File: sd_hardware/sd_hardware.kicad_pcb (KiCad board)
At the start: 2 copper layers, 103 x 70.5 mm, 87 parts, among them IC1 TJA1441AT, IC101 BD9E201FP4-Z, J1 Conn_01x02_Socket, J10 RJ45, J11 XT60PW-M_1x02_Horizontal, J12 Conn_01x02_Socket, J2 Conn_01x02_Socket, J3 Conn_01x02_Socket, J301 STLink-v3mini, J4 Conn_01x02_Socket, J5 Conn_01x02_Socket, J6 Conn_01x02_Socket, J7 Conn_01x02_Socket, J8 Conn_01x02_Socket, J9 RJ45, Q1 RD3L08BGNTL, Q2 RD3L08BGNTL, Q3 RD3L08BGNTL, Q4 RD3L08BGNTL, Q5 RD3L08BGNTL, Q6 RD3L08BGNTL, Q7 RD3L08BGNTL, Q8 RD3L08BGNTL, SW1 SW_DIP_x03, SW301 SW_Push, U1 TLP291, U2 TLP291, U3 TLP291, U301 STM32G431K8Tx, U4 TLP291, U5 TLP291, U6 TLP291, U7 TLP291, U8 TLP291

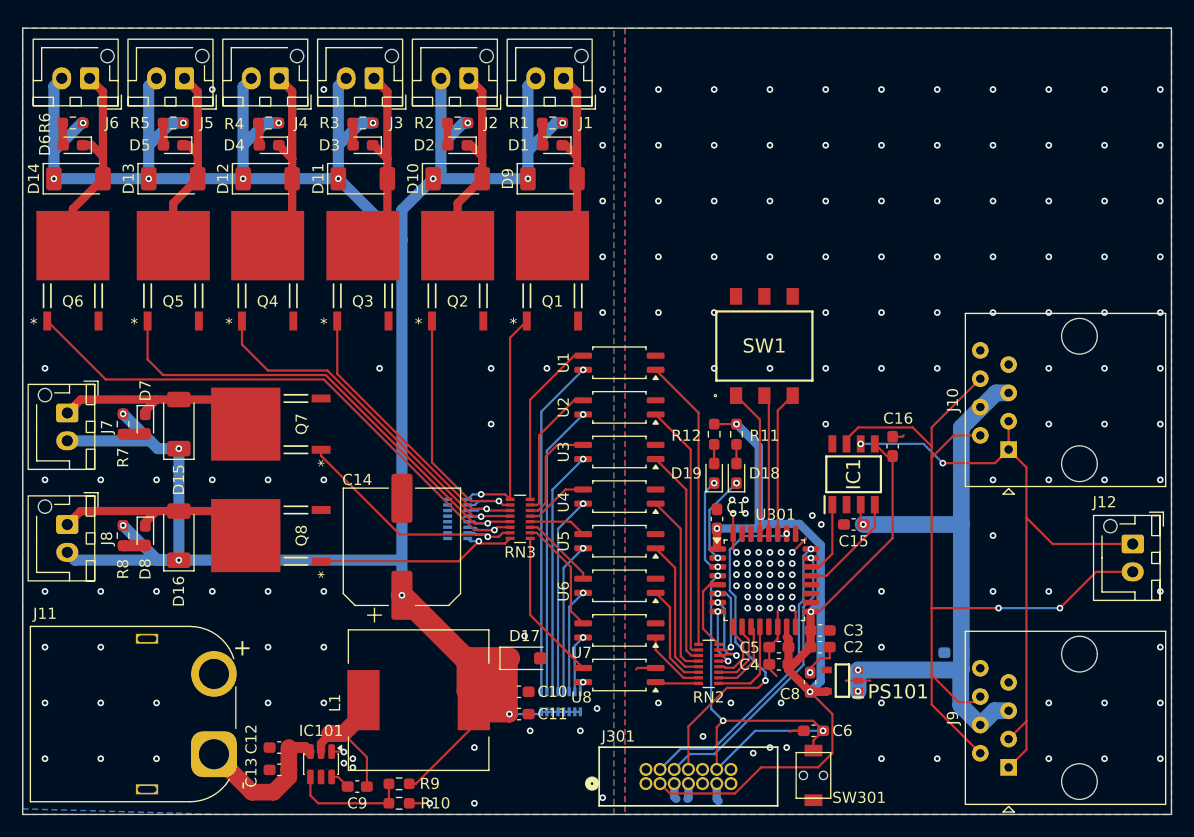
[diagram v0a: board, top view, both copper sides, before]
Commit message: fix var3.0 sd_hardware
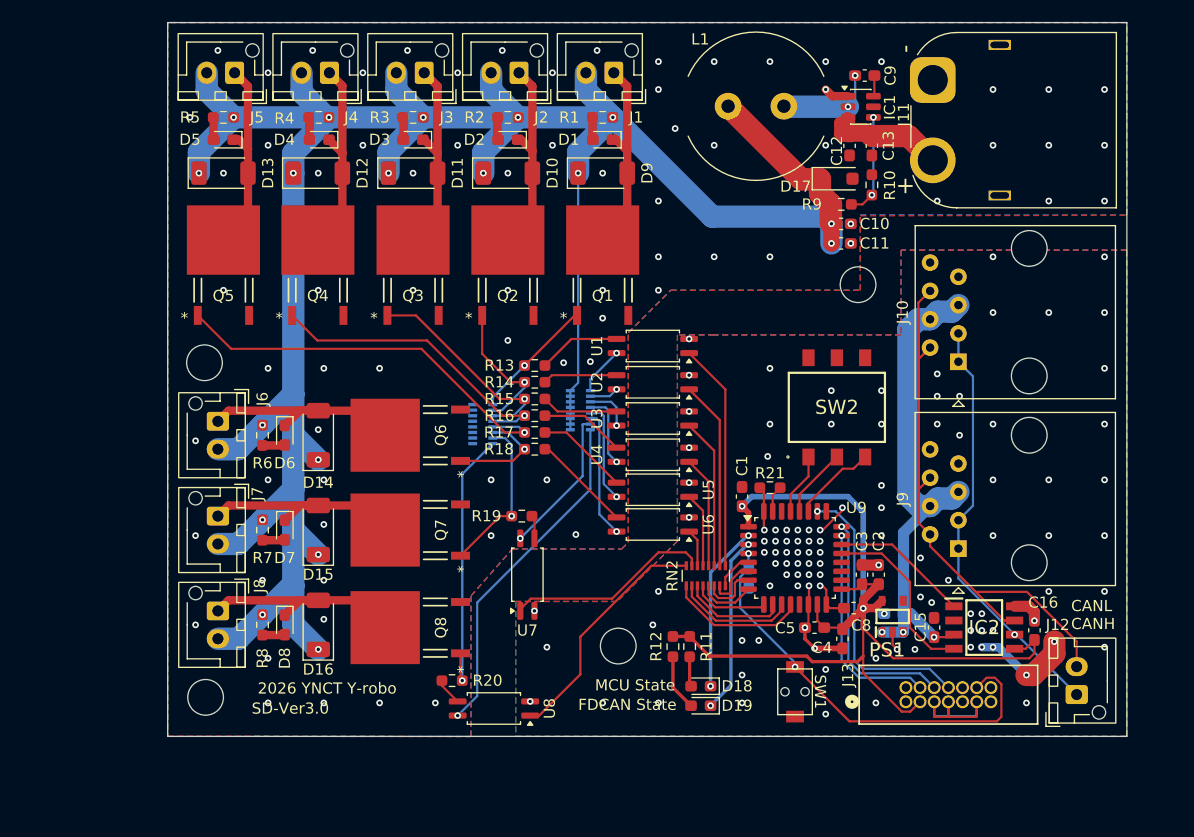
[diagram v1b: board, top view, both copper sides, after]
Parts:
- removed C14: 680μ, Capacitor_SMD:CP_Elec_10x12.6
- removed the RN3 at (127.6, 103.5)
- added R13: 120, Resistor_SMD:R_0603_1608Metric_Pad0.98x0.95mm_HandSolder, F.Cu at (128.9, 89.8)
- added R14: 120, Resistor_SMD:R_0603_1608Metric_Pad0.98x0.95mm_HandSolder, F.Cu at (128.9, 91.2)
- added R15: 120, Resistor_SMD:R_0603_1608Metric_Pad0.98x0.95mm_HandSolder, F.Cu at (128.9, 92.7)
- added R16: 120, Resistor_SMD:R_0603_1608Metric_Pad0.98x0.95mm_HandSolder, F.Cu at (128.9, 94.2)
- added R17: 120, Resistor_SMD:R_0603_1608Metric_Pad0.98x0.95mm_HandSolder, F.Cu at (128.9, 95.8)
- added R18: 120, Resistor_SMD:R_0603_1608Metric_Pad0.98x0.95mm_HandSolder, F.Cu at (128.9, 97.2)
- added R19: 120, Resistor_SMD:R_0603_1608Metric_Pad0.98x0.95mm_HandSolder, F.Cu at (127.8, 103.2)
- added R20: 120, Resistor_SMD:R_0603_1608Metric_Pad0.98x0.95mm_HandSolder, F.Cu at (121.5, 118.0)
- added R21: 10k, Resistor_SMD:R_0603_1608Metric_Pad0.98x0.95mm_HandSolder, F.Cu at (150.0, 100.7)
- added REF**: Y-robo_logo, y-robo_footprint:Y-robo_logo, B.Cu at (107.1, 69.7)
- C6: moved to B.Cu
- D17: value SMF24VTF -> SMF15VTF
- L1: footprint Inductor_SMD:L_12x12mm_H4.5mm -> y-robo_footprint:RP1315BNP-220M
- R1, R2, R3, R4, R5, R6, R7, R8: value 1k -> 1.5k
- moved J11 88.4 mm to (164.6, 64.2), turned to -90 degrees
- moved C9 78.3 mm to (158.5, 63.8), turned to 0 degrees
- moved C13 77.2 mm to (159.1, 70.0), turned to -90 degrees
- moved IC1 76.3 mm to (158.1, 66.5), turned to 0 degrees
- moved C12 74.3 mm to (157.1, 70.0), turned to -90 degrees
- moved R10 69.8 mm to (159.1, 73.5), turned to 90 degrees
- moved R9 65.3 mm to (156.4, 75.3), turned to 0 degrees
- moved L1 61.2 mm to (148.8, 66.5), turned to 0 degrees
- moved D17 51.3 mm to (156.0, 73.0)
- moved C11 51.1 mm to (156.4, 78.8)
- moved C10 50.9 mm to (156.4, 77.0)
- moved J6 32.8 mm to (100.5, 94.8), turned to -90 degrees
- moved Q6 32.8 mm to (115.5, 96.0), turned to 90 degrees
- moved R6 32.8 mm to (104.5, 96.0), turned to 90 degrees
- moved D6 32.2 mm to (106.5, 96.0), turned to -90 degrees
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- renumbered IC101 to IC1, IC1 to IC2, J301 to J13, PS101 to PS1, RN4 to RN3, SW301 to SW1, SW1 to SW2, U301 to U9
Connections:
- J11 pad 1: +24V -> GNDPWR
- J11 pad 2: GNDPWR -> +24V
- U9 pad 23: /MCU_stm32_g431k8t6/JTCK_SWCLK -> /MCU_stm32_g431k8t6/JTMS_SWDIO
- U9 pad 24: /MCU_stm32_g431k8t6/JTMS_SWDIO -> /MCU_stm32_g431k8t6/JTCK_SWCLK
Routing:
- net +12V: track 284.8 -> 233.0 mm
- net /Solenoid_Isolation/FET6_Gate: track 51.9 -> 9.65 mm
- net Net-(RN1-R1.2): track 0.97 -> 30.6 mm
- net /CANH: track 76.3 -> 50.2 mm, vias 2 -> 0
- net Net-(RN1-R8.2): track 30.4 -> 4.34 mm
- net Net-(RN1-R7.2): track 26.2 -> 2.60 mm
- net /CANL: track 59.6 -> 38.0 mm, vias 2 -> 1
- net GND: track 28.6 -> 50.2 mm, vias 129 -> 107
- net Net-(RN1-R6.2): track 22.0 -> 4.19 mm
- net Net-(RN2-R1.2): track 3.90 -> 21.5 mm
- net Net-(RN2-R2.2): track 6.00 -> 18.5 mm
- net +5V: track 57.4 -> 45.4 mm
- net /Solenoid_Isolation/FET2_Gate: track 24.3 -> 12.5 mm
- net Net-(RN1-R5.2): track 17.8 -> 6.65 mm
- net Net-(R20-Pad2): track 13.6 -> 2.45 mm
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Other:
- board size 103 x 70.5 mm -> 86 x 64 mm
- board text added: "2026 YNCT Y-robo"
- board text added: "CANL CANH"
- board text added: "FDCAN State"
- board text added: "MCU State"
- board text added: "SD-Ver3.0"

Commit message: created schematic
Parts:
- removed the C1 at (147.5, 101.5)
- removed the C2 at (159.8, 108.5)
- removed the C3 at (158.2, 108.5)
- removed the C4 at (156.5, 114.2)
- removed the C5 at (154.0, 113.2)
- removed the D3 at (118.0, 69.5)
- removed the IC1 at (158.1, 66.5)
- removed the L1 at (148.8, 66.5)
- removed Q1, Q2, Q3, Q4, Q5, Q6, Q7, Q8: RD3L08BGNTL, y-robo_footprint:TO252-3_ROM
- removed the R3 at (118.0, 67.5)
- removed the R4 at (109.5, 67.5)
- removed REF**: Y-robo_logo, y-robo_footprint:Y-robo_logo
- removed RN1: 1k_x8, Resistor_SMD:R_Array_Convex_8x0602
- removed RN2: 330_x8, Resistor_SMD:R_Array_Convex_8x0602
- removed RN3: 10k_x08, Resistor_SMD:R_Array_Convex_8x0602
- removed U7, U8: TLP291, Package_SO:SOIC-4_4.55x2.6mm_P1.27mm
- removed U9: STM32G431K8Tx, Package_QFP:LQFP-32_7x7mm_P0.8mm
- added C1: 0.1μ, Capacitor_SMD:C_0603_1608Metric_Pad1.08x0.95mm_HandSolder, F.Cu at (20.2, 123.0)
- added C1: 0.1μ, Capacitor_SMD:C_0603_1608Metric_Pad1.08x0.95mm_HandSolder, F.Cu at (94.8, 2.75)
- added C14: 0.1μ, Capacitor_SMD:C_0603_1608Metric_Pad1.08x0.95mm_HandSolder, F.Cu at (76.6, 66.9)
- added C17: 1μ, Capacitor_SMD:C_0603_1608Metric_Pad1.08x0.95mm_HandSolder, F.Cu at (72.5, 122.3)
- added C18: 220nF, Capacitor_SMD:C_0603_1608Metric_Pad1.08x0.95mm_HandSolder, F.Cu at (72.5, 124.8)
- added C19: 0.1μ, Capacitor_SMD:C_0603_1608Metric_Pad1.08x0.95mm_HandSolder, F.Cu at (72.5, 100.2)
- added C2: 22μ, Capacitor_SMD:C_0603_1608Metric_Pad1.08x0.95mm_HandSolder, F.Cu at (20.2, 125.5)
- added C2: 22μ, Capacitor_SMD:C_0603_1608Metric_Pad1.08x0.95mm_HandSolder, F.Cu at (92.6, 16.1)
- added C20: 0.1μ, Capacitor_SMD:C_0603_1608Metric_Pad1.08x0.95mm_HandSolder, F.Cu at (72.5, 102.7)
- added C21: 0.1μ, Capacitor_SMD:C_0603_1608Metric_Pad1.08x0.95mm_HandSolder, F.Cu at (76.6, 43.3)
- added C22: 0.1μ, Capacitor_SMD:C_0603_1608Metric_Pad1.08x0.95mm_HandSolder, F.Cu at (76.6, 45.8)
- added C23: 10nF, Capacitor_SMD:C_0603_1608Metric_Pad1.08x0.95mm_HandSolder, F.Cu at (76.6, 48.3)
- added C3: 22μ, Capacitor_SMD:C_0603_1608Metric_Pad1.08x0.95mm_HandSolder, F.Cu at (20.2, 128.0)
- added C3: 22μ, Capacitor_SMD:C_0603_1608Metric_Pad1.08x0.95mm_HandSolder, F.Cu at (92.6, 17.8)
- added C4: 0.1μ, Capacitor_SMD:C_0603_1608Metric_Pad1.08x0.95mm_HandSolder, F.Cu at (20.2, 130.5)
- added C4: 0.1μ, Capacitor_SMD:C_0603_1608Metric_Pad1.08x0.95mm_HandSolder, F.Cu at (93.4, 9.05)
- added C5: 10μ, Capacitor_SMD:C_0603_1608Metric_Pad1.08x0.95mm_HandSolder, F.Cu at (95.4, 9.05)
- added C5: 10μ, Capacitor_SMD:C_0603_1608Metric_Pad1.08x0.95mm_HandSolder, F.Cu at (20.2, 133.0)
- added D3: SMF15VTF, Diode_SMD:D_SOD-123F, F.Cu at (92.2, 12.0)
- added D3: SMF15VTF, Diode_SMD:D_SOD-123F, F.Cu at (44.2, 131.2)
- added IC1: BD9E201FP4-Z, Package_TO_SOT_SMD:TSOT-23-6, F.Cu at (94.4, 5.55)
- added IC1: BD9E201FP4-Z, Package_TO_SOT_SMD:TSOT-23-6, F.Cu at (38.9, 131.9)
- added IC10: TJA1441AT, y-robo_footprint:SOIC127P600X175-8N, F.Cu at (78.7, 62.3)
- added IC3: TLP170AM_TPL,E, y-robo_footprint:TLP170AMTPLE, F.Cu at (28.2, 47.3)
- added IC4: TLP170AM_TPL,E, y-robo_footprint:TLP170AMTPLE, F.Cu at (35.0, 47.3)
- added IC5: TLP170AM_TPL,E, y-robo_footprint:TLP170AMTPLE, F.Cu at (41.8, 47.3)
- added IC6: TLP170AM_TPL,E, y-robo_footprint:TLP170AMTPLE, F.Cu at (48.6, 47.3)
- added IC7: TLP170AM_TPL,E, y-robo_footprint:TLP170AMTPLE, F.Cu at (55.4, 47.3)
- added IC8: TLP170AM_TPL,E, y-robo_footprint:TLP170AMTPLE, F.Cu at (62.2, 47.3)
- added IC9: TLP170AM_TPL,E, y-robo_footprint:TLP170AMTPLE, F.Cu at (69.0, 47.3)
- added J14: STLink-v3mini, y-robo_footprint:CONN14_3220-14_CNC, F.Cu at (84.4, 93.3)
- added L1: 22μ, y-robo_footprint:RP1315BNP-220M, F.Cu at (85.0, 5.50)
- added L1: 22μ, y-robo_footprint:RP1315BNP-220M, F.Cu at (60.7, 109.3)
- added R22: 1.5k, Resistor_SMD:R_0603_1608Metric_Pad0.98x0.95mm_HandSolder, F.Cu at (38.4, 61.7)
- added R23: 10k, Resistor_SMD:R_0603_1608Metric_Pad0.98x0.95mm_HandSolder, F.Cu at (38.4, 64.2)
- added R24: 10k, Resistor_SMD:R_0603_1608Metric_Pad0.98x0.95mm_HandSolder, F.Cu at (38.4, 66.8)
- added R25: 10k, Resistor_SMD:R_0603_1608Metric_Pad0.98x0.95mm_HandSolder, F.Cu at (42.7, 54.2)
- added R26: 10k, Resistor_SMD:R_0603_1608Metric_Pad0.98x0.95mm_HandSolder, F.Cu at (42.7, 56.7)
- added R27: 10k, Resistor_SMD:R_0603_1608Metric_Pad0.98x0.95mm_HandSolder, F.Cu at (42.7, 59.2)
- added R28: 10k, Resistor_SMD:R_0603_1608Metric_Pad0.98x0.95mm_HandSolder, F.Cu at (42.7, 61.7)
- added R29: 10k, Resistor_SMD:R_0603_1608Metric_Pad0.98x0.95mm_HandSolder, F.Cu at (42.7, 64.2)
- added R3: 100k, Resistor_SMD:R_0603_1608Metric_Pad0.98x0.95mm_HandSolder, F.Cu at (24.5, 133.0)
- added R3: 100k, Resistor_SMD:R_0603_1608Metric_Pad0.98x0.95mm_HandSolder, F.Cu at (92.6, 14.3)
- added R30: 10k, Resistor_SMD:R_0603_1608Metric_Pad0.98x0.95mm_HandSolder, F.Cu at (42.7, 66.8)
- added R31: 10k, Resistor_SMD:R_0603_1608Metric_Pad0.98x0.95mm_HandSolder, F.Cu at (72.5, 94.9)
- added R32: 0, Resistor_SMD:R_0603_1608Metric_Pad0.98x0.95mm_HandSolder, F.Cu at (72.5, 127.3)
- added R33: 0, Resistor_SMD:R_0603_1608Metric_Pad0.98x0.95mm_HandSolder, F.Cu at (72.5, 129.8)
- added R34: 40k, Resistor_SMD:R_0603_1608Metric_Pad0.98x0.95mm_HandSolder, F.Cu at (72.5, 132.3)
- added R35: 40k, Resistor_SMD:R_0603_1608Metric_Pad0.98x0.95mm_HandSolder, F.Cu at (76.8, 119.8)
- added R36: 0, Resistor_SMD:R_0603_1608Metric_Pad0.98x0.95mm_HandSolder, F.Cu at (76.8, 122.3)
- added R37: 10k, Resistor_SMD:R_0603_1608Metric_Pad0.98x0.95mm_HandSolder, F.Cu at (76.8, 124.8)
- added R38: 0, Resistor_SMD:R_0603_1608Metric_Pad0.98x0.95mm_HandSolder, F.Cu at (76.8, 127.3)
- added R39: 10k, Resistor_SMD:R_0603_1608Metric_Pad0.98x0.95mm_HandSolder, F.Cu at (76.8, 129.8)
- added R4: 5.23k, Resistor_SMD:R_0603_1608Metric_Pad0.98x0.95mm_HandSolder, F.Cu at (28.9, 123.0)
- added R4: 5.23k, Resistor_SMD:R_0603_1608Metric_Pad0.98x0.95mm_HandSolder, F.Cu at (95.4, 12.6)
- added R40: 10k, Resistor_SMD:R_0603_1608Metric_Pad0.98x0.95mm_HandSolder, F.Cu at (72.5, 105.2)
- added R41: 10k, Resistor_SMD:R_0603_1608Metric_Pad0.98x0.95mm_HandSolder, F.Cu at (72.5, 107.7)
- added R42: 0, Resistor_SMD:R_0603_1608Metric_Pad0.98x0.95mm_HandSolder, F.Cu at (72.5, 110.3)
- added R43: 0, Resistor_SMD:R_0603_1608Metric_Pad0.98x0.95mm_HandSolder, F.Cu at (72.5, 112.8)
- added R44: 0, Resistor_SMD:R_0603_1608Metric_Pad0.98x0.95mm_HandSolder, F.Cu at (72.5, 115.3)
- added R45: 100k, Resistor_SMD:R_0603_1608Metric_Pad0.98x0.95mm_HandSolder, F.Cu at (76.6, 50.8)
- added R46: 100, Resistor_SMD:R_0603_1608Metric_Pad0.98x0.95mm_HandSolder, F.Cu at (76.6, 53.3)
- added R47: 100k, Resistor_SMD:R_0603_1608Metric_Pad0.98x0.95mm_HandSolder, F.Cu at (76.6, 55.8)
- C10: value 22μ -> 100n
- C11: value 22μ -> 1μ
- C12: value 0.1μ -> 10n
- C13: value 10μ -> 0.1μ
- C15: value 0.1μ -> 0.1u
- C16: value 0.1u -> 0.1μ
- C6: value 0.1μ -> 1μ; moved to F.Cu
- C7: moved to F.Cu
- C8: value 1μ -> 100n
- C9: value 0.1μ -> 4.7μ
- D10, D12, D14, D16: value RB055LAM-40TR -> LED; footprint Diode_SMD:D_SOD-128 -> LED_SMD:LED_0603_1608Metric_Pad1.05x0.95mm_HandSolder
- D11, D13, D15, D9: value RB055LAM-40TR -> RB520VM-40; footprint Diode_SMD:D_SOD-128 -> Diode_SMD:D_SOD-323_HandSoldering
- D17: value SMF15VTF -> RB520VM-40; footprint Diode_SMD:D_SOD-123F -> Diode_SMD:D_SOD-323_HandSoldering
- D19, D5, D7: value LED -> RB520VM-40; footprint LED_SMD:LED_0603_1608Metric_Pad1.05x0.95mm_HandSolder -> Diode_SMD:D_SOD-323_HandSoldering
- IC2: value TJA1441AT -> TLP170AM_TPL,E; footprint y-robo_footprint:SOIC127P600X175-8N -> y-robo_footprint:TLP170AMTPLE
- J1: footprint Connector_JST:JST_XH_B2B-XH-AM_1x02_P2.50mm_Vertical -> Connector_JST:JST_XH_B2B-XH-A_1x02_P2.50mm_Vertical
- J10: value RJ45 -> Conn_01x06_Socket; footprint Connector_RJ:RJ45_Amphenol_54602-x08_Horizontal -> Connector_JST:JST_XH_B6B-XH-A_1x06_P2.50mm_Vertical
- J11: value XT60PW-M_1x02_Horizontal -> Conn_01x02_Socket; footprint Connector_AMASS:AMASS_XT60PW-M_1x02_P7.20mm_Horizontal -> Connector_JST:JST_XH_B2B-XH-AM_1x02_P2.50mm_Vertical
- J12: value Conn_01x02_Socket -> RJ45; footprint Connector_JST:JST_XH_B2B-XH-AM_1x02_P2.50mm_Vertical -> Connector_RJ:RJ45_Amphenol_54602-x08_Horizontal
- J13: value STLink-v3mini -> RJ45; footprint y-robo_footprint:CONN14_3220-14_CNC -> Connector_RJ:RJ45_Amphenol_54602-x08_Horizontal
- J8: value Conn_01x02_Socket -> XT60PW-M_1x02_Horizontal; footprint Connector_JST:JST_XH_B2B-XH-AM_1x02_P2.50mm_Vertical -> Connector_AMASS:AMASS_XT60PW-M_1x02_P7.20mm_Horizontal
- J9: value RJ45 -> Conn_01x02_Socket; footprint Connector_RJ:RJ45_Amphenol_54602-x08_Horizontal -> Connector_JST:JST_XH_B2B-XH-AM_1x02_P2.50mm_Vertical
- R1, R2: value 1.5k -> 1k
- R10: value 5.23k -> 680
- R11, R12: value 1k -> 680
- R13, R14, R15, R16: value 120 -> 680
- R17, R18, R19, R20: value 120 -> 1.5k
- R21: value 10k -> 1.5k
- R5, R6: value 1.5k -> 0
- R9: value 100k -> 680
- SW1: value SW_Push -> SW_DIP_x03; footprint y-robo_footprint:TVAF06-A020B-R -> y-robo_footprint:DS04-254-2-03BK-SMT
- SW2: value SW_DIP_x03 -> SW_Push; footprint y-robo_footprint:DS04-254-2-03BK-SMT -> y-robo_footprint:TVAF06-A020B-R
- U1: value TLP291 -> STM32G431K8Tx; footprint Package_SO:SOIC-4_4.55x2.6mm_P1.27mm -> Package_QFP:LQFP-32_7x7mm_P0.8mm
- U2: value TLP291 -> DAC60501ZDGSR; footprint Package_SO:SOIC-4_4.55x2.6mm_P1.27mm -> y-robo_footprint:DGS10_TEX
- U3: value TLP291 -> BD87521G-LB; footprint Package_SO:SOIC-4_4.55x2.6mm_P1.27mm -> y-robo_footprint:SOT95P280X125-5N
- U4: value TLP291 -> ADUM251N1BRIZ; footprint Package_SO:SOIC-4_4.55x2.6mm_P1.27mm -> y-robo_footprint:ADUM251N1BRIZ_ADI
- U5: value TLP291 -> BD87581YG-C; footprint Package_SO:SOIC-4_4.55x2.6mm_P1.27mm -> y-robo_footprint:SOT95P280X125-5N
- U6: value TLP291 -> ADS1018IDGSR; footprint Package_SO:SOIC-4_4.55x2.6mm_P1.27mm -> y-robo_footprint:DGS10_TEX
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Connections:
- C10 pad 1: +12V -> +3.3V
- C10 pad 2: GNDPWR -> GND
- C11 pad 1: +12V -> +3.3V
- C11 pad 2: GNDPWR -> GND
- C12 pad 1: +24V -> +3.3V
- C12 pad 2: GNDPWR -> GND
- C13 pad 1: +24V -> /MCU_stm32_g431k8t6/NRST
- C13 pad 2: GNDPWR -> GND
- C15 pad 1: +5V -> +3.3V
- C16 pad 1: +3.3V -> +12V
- C16 pad 2: GND -> GNDPWR
- C6 pad 1: /MCU_stm32_g431k8t6/NRST -> +5V
- C7 pad 1: +5V -> +3.3V
- C9 pad 1: Net-(IC1-SW) -> +3.3V
- C9 pad 2: Net-(IC1-BOOT) -> GND
- D1 pad 1: /Solenoid_Isolation/Solenoid1_- -> /MCU_stm32_g431k8t6/MCU_State_LED
- D10 pad 1: +12V -> /Solenoid_Iso/PhotoRelay6_Drain
- D10 pad 2: /Solenoid_Isolation/Solenoid2_- -> Net-(D10-A)
- D11 pad 2: /Solenoid_Isolation/Solenoid3_- -> /Solenoid_Iso/PhotoRelay6_Drain
- D12 pad 1: +12V -> /Solenoid_Iso/PhotoRelay3_Drain
- D12 pad 2: /Solenoid_Isolation/Solenoid4_- -> Net-(D12-A)
- D13 pad 2: /Solenoid_Isolation/Solenoid5_- -> /Solenoid_Iso/PhotoRelay3_Drain
- D14 pad 1: +12V -> /Solenoid_Iso/PhotoRelay7_Drain
- D14 pad 2: /Solenoid_Isolation/Solenoid6_- -> Net-(D14-A)
- D15 pad 2: /Solenoid_Isolation/Solenoid7_- -> /Solenoid_Iso/PhotoRelay7_Drain
- D16 pad 1: +12V -> /Solenoid_Iso/PhotoRelay4_Drain
- D16 pad 2: /Solenoid_Isolation/Solenoid8_- -> Net-(D16-A)
- D17 pad 2: GNDPWR -> /Solenoid_Iso/PhotoRelay4_Drain
- D18 pad 1: /MCU_stm32_g431k8t6/MCU_State_LED -> /Solenoid_Iso/PhotoRelay8_Drain
- D19 pad 1: /MCU_stm32_g431k8t6/FDCAN1_LED -> +12V
- D19 pad 2: Net-(D19-A) -> /Solenoid_Iso/PhotoRelay8_Drain
- D2 pad 1: /Solenoid_Isolation/Solenoid2_- -> /MCU_stm32_g431k8t6/FDCAN1_LED
- D4 pad 1: /Solenoid_Isolation/Solenoid4_- -> /Solenoid_Iso/PhotoRelay1_Drain
- D5 pad 1: /Solenoid_Isolation/Solenoid5_- -> +12V
- D5 pad 2: Net-(D5-A) -> /Solenoid_Iso/PhotoRelay1_Drain
- D6 pad 1: /Solenoid_Isolation/Solenoid6_- -> /Solenoid_Iso/PhotoRelay5_Drain
- D7 pad 1: /Solenoid_Isolation/Solenoid7_- -> +12V
- D7 pad 2: Net-(D7-A) -> /Solenoid_Iso/PhotoRelay5_Drain
- D8 pad 1: /Solenoid_Isolation/Solenoid8_- -> /Solenoid_Iso/PhotoRelay2_Drain
- D9 pad 2: /Solenoid_Isolation/Solenoid1_- -> /Solenoid_Iso/PhotoRelay2_Drain
- IC2 pad 1: /FDCAN_Transceiver/CAN_TX -> Net-(IC2-A)
- IC2 pad 3: +5V -> GND
- IC2 pad 4: /FDCAN_Transceiver/CAN_RX -> GNDPWR
- IC2 pad 6: /CANL -> /Solenoid_Iso/PhotoRelay1_Drain
- J1 pad 1: /Solenoid_Isolation/Solenoid1_- -> /Solenoid_Iso/PhotoRelay1_Drain
- J10 pad 1: /CANL -> +12V
- J10 pad 2: /CANH -> GNDPWR
- J10 pad 3: /CANL -> /SPI_DAC/-VSENSE
- J10 pad 4: +5V -> /SPI_DAC/VOUT
- J10 pad 5: +5V -> /SPI_DAC/+VSENSE
- J10 pad 6: /CANH -> /SPI_ADC/VIN
- J11 pad 1: GNDPWR -> /CANL
- J11 pad 2: +24V -> /CANH
- J13 pad 1: unconnected-(J13-Pin_1-Pad1) -> /CANL
- J13 pad 2: unconnected-(J13-Pin_2-Pad2) -> /CANH
- J13 pad 3: +3.3V -> /CANL
- J13 pad 4: /MCU_stm32_g431k8t6/JTMS_SWDIO -> +5V
- J13 pad 5: GND -> +5V
- J13 pad 6: /MCU_stm32_g431k8t6/JTCK_SWCLK -> /CANH
- J13 pad 8: /MCU_stm32_g431k8t6/JTDO_SWO -> GND
- J2 pad 1: /Solenoid_Isolation/Solenoid2_- -> /Solenoid_Iso/PhotoRelay5_Drain
- J3 pad 1: /Solenoid_Isolation/Solenoid3_- -> /Solenoid_Iso/PhotoRelay2_Drain
- J4 pad 1: /Solenoid_Isolation/Solenoid4_- -> /Solenoid_Iso/PhotoRelay6_Drain
- J5 pad 1: /Solenoid_Isolation/Solenoid5_- -> /Solenoid_Iso/PhotoRelay3_Drain
- J6 pad 1: /Solenoid_Isolation/Solenoid6_- -> /Solenoid_Iso/PhotoRelay7_Drain
- J7 pad 1: /Solenoid_Isolation/Solenoid7_- -> /Solenoid_Iso/PhotoRelay4_Drain
- J8 pad 1: /Solenoid_Isolation/Solenoid8_- -> GNDPWR
- J8 pad 2: +12V -> +24V
- J9 pad 1: /CANL -> /Solenoid_Iso/PhotoRelay8_Drain
- J9 pad 2: /CANH -> +12V
- R1 pad 1: Net-(D1-A) -> +3.3V
- R1 pad 2: +12V -> Net-(D1-A)
- R10 pad 1: /FB -> /MCU_stm32_g431k8t6/Solenoid2_GPIO
- R10 pad 2: GNDPWR -> Net-(IC3-A)
- R11 pad 1: +3.3V -> /MCU_stm32_g431k8t6/Solenoid3_GPIO
- R11 pad 2: Net-(D18-A) -> Net-(IC4-A)
- R12 pad 1: +3.3V -> /MCU_stm32_g431k8t6/Solenoid4_GPIO
- R12 pad 2: Net-(D19-A) -> Net-(IC5-A)
- R13 pad 1: /Solenoid_Isolation/FET1_Gate -> /MCU_stm32_g431k8t6/Solenoid5_GPIO
- R13 pad 2: Net-(R13-Pad2) -> Net-(IC6-A)
- R14 pad 1: /Solenoid_Isolation/FET2_Gate -> /MCU_stm32_g431k8t6/Solenoid6_GPIO
- R14 pad 2: Net-(R14-Pad2) -> Net-(IC7-A)
- R15 pad 1: /Solenoid_Isolation/FET3_Gate -> /MCU_stm32_g431k8t6/Solenoid7_GPIO
- R15 pad 2: Net-(R15-Pad2) -> Net-(IC8-A)
- R16 pad 1: /Solenoid_Isolation/FET4_Gate -> /MCU_stm32_g431k8t6/Solenoid8_GPIO
- R16 pad 2: Net-(R16-Pad2) -> Net-(IC9-A)
- R17 pad 1: /Solenoid_Isolation/FET5_Gate -> Net-(D8-A)
- R17 pad 2: Net-(R17-Pad2) -> +12V
- R18 pad 1: /Solenoid_Isolation/FET6_Gate -> Net-(D10-A)
- R18 pad 2: Net-(R18-Pad2) -> +12V
- R19 pad 1: /Solenoid_Isolation/FET7_Gate -> Net-(D12-A)
- R19 pad 2: Net-(R19-Pad2) -> +12V
- R2 pad 1: Net-(D2-A) -> +3.3V
- R2 pad 2: +12V -> Net-(D2-A)
- R20 pad 1: /Solenoid_Isolation/FET8_Gate -> Net-(D14-A)
- R20 pad 2: Net-(R20-Pad2) -> +12V
- R21 pad 1: /MCU_stm32_g431k8t6/BOOT0 -> Net-(D16-A)
- R21 pad 2: GND -> +12V
- R5 pad 1: Net-(D5-A) -> /MCU_stm32_g431k8t6/SPI1_SCK
- R5 pad 2: +12V -> /SPI_Iso/CLK_IN
- R6 pad 1: Net-(D6-A) -> /MCU_stm32_g431k8t6/SPI1_MOSI
- R6 pad 2: +12V -> /SPI_Iso/MOSI_IN
- R7 pad 1: Net-(D7-A) -> Net-(D4-A)
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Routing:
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- removed copper zone on B.Cu, net GND
- removed copper zone on F.Cu, net GND
- removed copper zone on B.Cu, net GNDPWR
- removed copper zone on F.Cu, net GNDPWR
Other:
- board outline removed
- board text removed: "2026 YNCT Y-robo"
- board text removed: "CANL CANH"
- board text removed: "FDCAN State"
- board text removed: "MCU State"
- board text removed: "SD-Ver3.0"

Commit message: working
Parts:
- removed the C1 at (20.2, 123.0)
- removed the C1 at (94.8, 2.75)
- removed the C2 at (20.2, 125.5)
- removed the C2 at (92.6, 16.1)
- removed the C3 at (20.2, 128.0)
- removed the C3 at (92.6, 17.8)
- removed the C4 at (20.2, 130.5)
- removed the C4 at (93.4, 9.05)
- removed the C5 at (95.4, 9.05)
- removed the C5 at (20.2, 133.0)
- removed the D3 at (92.2, 12.0)
- removed the D3 at (44.2, 131.2)
- removed the IC1 at (94.4, 5.55)
- removed the IC1 at (38.9, 131.9)
- removed the L1 at (85.0, 5.50)
- removed the L1 at (60.7, 109.3)
- removed the R3 at (24.5, 133.0)
- removed the R3 at (92.6, 14.3)
- removed the R4 at (28.9, 123.0)
- removed the R4 at (95.4, 12.6)
- added C1: 0.1μ, Capacitor_SMD:C_0603_1608Metric_Pad1.08x0.95mm_HandSolder, F.Cu at (130.9, 50.0)
- added C2: 0.1μ, Capacitor_SMD:C_0603_1608Metric_Pad1.08x0.95mm_HandSolder, F.Cu at (141.8, 59.0)
- added C24: 0.1μ, Capacitor_SMD:C_0603_1608Metric_Pad1.08x0.95mm_HandSolder, B.Cu at (99.9, 60.8)
- added C25: 10nF, Capacitor_SMD:C_0603_1608Metric_Pad1.08x0.95mm_HandSolder, B.Cu at (96.4, 65.3)
- added C3: 0.1μ, Capacitor_SMD:C_0603_1608Metric_Pad1.08x0.95mm_HandSolder, B.Cu at (123.2, 55.8)
- added C4: 4.7μ, Capacitor_SMD:C_0603_1608Metric_Pad1.08x0.95mm_HandSolder, F.Cu at (141.8, 60.5)
- added C5: 1μ, Capacitor_SMD:C_0603_1608Metric_Pad1.08x0.95mm_HandSolder, F.Cu at (138.1, 62.5)
- added D20: LED, LED_SMD:LED_0603_1608Metric_Pad1.05x0.95mm_HandSolder, F.Cu at (129.2, 73.5)
- added D21: LED, LED_SMD:LED_0603_1608Metric_Pad1.05x0.95mm_HandSolder, F.Cu at (114.0, 73.0)
- added D3: RB520VM-40, Diode_SMD:D_SOD-323_HandSoldering, F.Cu at (144.8, 30.2)
- added IC1: TLP170AM_TPL,E, y-robo_footprint:TLP170AMTPLE, F.Cu at (162.8, 37.8)
- added L1: 22μ, y-robo_footprint:RP1315BNP-220M, F.Cu at (90.5, 41.2)
- added R3: 3.3k, Resistor_SMD:R_0603_1608Metric_Pad0.98x0.95mm_HandSolder, F.Cu at (144.8, 26.2)
- added R4: 3.3k, Resistor_SMD:R_0603_1608Metric_Pad0.98x0.95mm_HandSolder, F.Cu at (135.8, 26.2)
- added R48: 100, Resistor_SMD:R_0603_1608Metric_Pad0.98x0.95mm_HandSolder, B.Cu at (96.4, 63.8)
- added R49: 100k, Resistor_SMD:R_0603_1608Metric_Pad0.98x0.95mm_HandSolder, B.Cu at (101.6, 60.8)
- added R50: 1k, Resistor_SMD:R_0603_1608Metric_Pad0.98x0.95mm_HandSolder, F.Cu at (132.7, 73.5)
- added R51: 1k, Resistor_SMD:R_0603_1608Metric_Pad0.98x0.95mm_HandSolder, F.Cu at (114.0, 71.2)
- added R52: 0, Resistor_SMD:R_0603_1608Metric_Pad0.98x0.95mm_HandSolder, B.Cu at (127.5, 60.8)
- added R53: 0, Resistor_SMD:R_0603_1608Metric_Pad0.98x0.95mm_HandSolder, F.Cu at (111.2, 60.5)
- added R54: 0, Resistor_SMD:R_0603_1608Metric_Pad0.98x0.95mm_HandSolder, F.Cu at (111.2, 62.0)
- added U7: BD00FC0WEFJ, Package_SO:HTSOP-8-1EP_3.9x4.9mm_P1.27mm_EP2.4x3.2mm, B.Cu at (90.8, 52.8)
- C10: value 100n -> 10μ
- C11: value 1μ -> 22μ
- C12: value 10n -> 22μ
- C13, C14: value 0.1μ -> 1μ; moved to B.Cu
- C15: value 0.1u -> 0.1μ
- C16, C7, IC10, PS1, R47, R9, U5, U6: moved to B.Cu
- C17: value 1μ -> 0.1u; moved to B.Cu
- C18: value 220nF -> 0.1μ
- C21: value 0.1μ -> 1μ
- C22: value 0.1μ -> 220nF
- C23: value 10nF -> 0.1μ; moved to B.Cu
- C6: value 1μ -> 10n
- C8: value 100n -> 1μ; moved to B.Cu
- C9: value 4.7μ -> 0.1μ
- D1, D2, D4, D6, D8: value LED -> RB520VM-40; footprint LED_SMD:LED_0603_1608Metric_Pad1.05x0.95mm_HandSolder -> Diode_SMD:D_SOD-323_HandSoldering
- D11, D13, D15, D17, D9: value RB520VM-40 -> LED; footprint Diode_SMD:D_SOD-323_HandSoldering -> LED_SMD:LED_0603_1608Metric_Pad1.05x0.95mm_HandSolder
- D19: value RB520VM-40 -> SMF15VTF; footprint Diode_SMD:D_SOD-323_HandSoldering -> Diode_SMD:D_SOD-123F
- IC9: value TLP170AM_TPL,E -> BD9E201FP4-Z; footprint y-robo_footprint:TLP170AMTPLE -> Package_TO_SOT_SMD:TSOT-23-6
- J10: value Conn_01x06_Socket -> RJ45; footprint Connector_JST:JST_XH_B6B-XH-A_1x06_P2.50mm_Vertical -> Connector_RJ:RJ45_Amphenol_54602-x08_Horizontal
- J11: value Conn_01x02_Socket -> RJ45; footprint Connector_JST:JST_XH_B2B-XH-AM_1x02_P2.50mm_Vertical -> Connector_RJ:RJ45_Amphenol_54602-x08_Horizontal
- J12: value RJ45 -> Conn_01x02_Socket; footprint Connector_RJ:RJ45_Amphenol_54602-x08_Horizontal -> Connector_JST:JST_XH_B2B-XH-A_1x02_P2.50mm_Vertical
- J13: value RJ45 -> XT60PW-M_1x02_Horizontal; footprint Connector_RJ:RJ45_Amphenol_54602-x08_Horizontal -> Connector_AMASS:AMASS_XT60PW-M_1x02_P7.20mm_Horizontal
- J14: value STLink-v3mini -> Conn_01x06_Socket; footprint y-robo_footprint:CONN14_3220-14_CNC -> Connector_JST:JST_XH_B6B-XH-A_1x06_P2.50mm_Vertical
- J2, J3, J4, J5, J6, J7: footprint Connector_JST:JST_XH_B2B-XH-AM_1x02_P2.50mm_Vertical -> Connector_JST:JST_XH_B2B-XH-A_1x02_P2.50mm_Vertical
- J8: value XT60PW-M_1x02_Horizontal -> Conn_01x02_Socket; footprint Connector_AMASS:AMASS_XT60PW-M_1x02_P7.20mm_Horizontal -> Connector_JST:JST_XH_B2B-XH-A_1x02_P2.50mm_Vertical
- J9: value Conn_01x02_Socket -> STLink-v3mini; footprint Connector_JST:JST_XH_B2B-XH-AM_1x02_P2.50mm_Vertical -> y-robo_footprint:CONN14_3220-14_CNC
- R1, R2: value 1k -> 3.3k
- R17: value 1.5k -> 10k; moved to B.Cu
- R18, R19, R20, R21, R22: value 1.5k -> 10k
- R26, R27: value 10k -> 1k
- R28, R29, R31: value 10k -> 0; moved to B.Cu
- R30, R39, R40: value 10k -> 0
- R33: value 0 -> 56.7k; moved to B.Cu
- R34: value 40k -> 10k; moved to B.Cu
- R35: value 40k -> 100k
- R36: value 0 -> 5.23k
- R38, R44: value 0 -> 10k
- R41: value 10k -> 40k; moved to B.Cu
- R42: value 0 -> 40k; moved to B.Cu
- R45: value 100k -> 0
- R46: value 100 -> 10k
- R5, R6: value 0 -> 3.3k
- R7, R8: value 1.5k -> 3.3k
- SW1: value SW_DIP_x03 -> SW_Push; footprint y-robo_footprint:DS04-254-2-03BK-SMT -> y-robo_footprint:TVAF06-A020B-R
- SW2: value SW_Push -> SW_DIP_x03; footprint y-robo_footprint:TVAF06-A020B-R -> y-robo_footprint:DS04-254-2-03BK-SMT
- U2: value DAC60501ZDGSR -> ADUM251N1BRIZ; footprint y-robo_footprint:DGS10_TEX -> y-robo_footprint:ADUM251N1BRIZ_ADI
- U3: value BD87521G-LB -> DAC60501ZDGSR; footprint y-robo_footprint:SOT95P280X125-5N -> y-robo_footprint:DGS10_TEX
- U4: value ADUM251N1BRIZ -> BD87521G-LB; footprint y-robo_footprint:ADUM251N1BRIZ_ADI -> y-robo_footprint:SOT95P280X125-5N
- moved R1 171.7 mm to (162.8, 26.2)
- moved R2 166.1 mm to (153.8, 26.2)
- moved J1 154.4 mm to (163.5, 21.3), turned to 180 degrees
- moved J2 149.8 mm to (154.8, 21.3), turned to 180 degrees
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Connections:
- C10 pad 1: +3.3V -> +24V
- C10 pad 2: GND -> GNDPWR
- C11 pad 1: +3.3V -> +12V
- C11 pad 2: GND -> GNDPWR
- C12 pad 1: +3.3V -> +12V
- C12 pad 2: GND -> GNDPWR
- C13 pad 1: /MCU_stm32_g431k8t6/NRST -> +24V
- C13 pad 2: GND -> GNDPWR
- C14 pad 1: +5V -> +5VP
- C14 pad 2: GND -> GNDPWR
- C15 pad 1: +3.3V -> Net-(IC9-SW)
- C15 pad 2: GND -> Net-(IC9-BOOT)
- C16 pad 1: +12V -> +5V
- C16 pad 2: GNDPWR -> GND
- C17 pad 1: +12V -> +3.3V
- C17 pad 2: GNDPWR -> GND
- C18 pad 1: Net-(U2-VREFIO) -> +3.3V
- C19 pad 1: +3.3V -> +5VP
- C19 pad 2: GND -> GNDPWR
- C20 pad 1: +5VP -> +12V
- C21 pad 1: +5VP -> +12V
- C22 pad 1: Net-(U5-+) -> Net-(U3-VREFIO)
- C23 pad 1: Net-(U6-AIN0) -> +5VP
- C6 pad 1: +5V -> +3.3V
- C7 pad 1: +3.3V -> +5V
- C9 pad 1: +3.3V -> +24V
- C9 pad 2: GND -> GNDPWR
- D1 pad 1: /MCU_stm32_g431k8t6/MCU_State_LED -> +12V
- D1 pad 2: Net-(D1-A) -> /Solenoid_Iso/PhotoRelay1_Drain
- D10 pad 1: /Solenoid_Iso/PhotoRelay6_Drain -> /Solenoid_Iso/Solenoid2_-
- D11 pad 1: +12V -> /Solenoid_Iso/PhotoRelay3_Drain
- D11 pad 2: /Solenoid_Iso/PhotoRelay6_Drain -> Net-(D11-A)
- D12 pad 1: /Solenoid_Iso/PhotoRelay3_Drain -> /Solenoid_Iso/PhotoRelay4_Drain
- D13 pad 1: +12V -> /Solenoid_Iso/PhotoRelay5_Drain
- D13 pad 2: /Solenoid_Iso/PhotoRelay3_Drain -> Net-(D13-A)
- D14 pad 1: /Solenoid_Iso/PhotoRelay7_Drain -> /Solenoid_Iso/PhotoRelay6_Drain
- D15 pad 1: +12V -> /Solenoid_Iso/PhotoRelay7_Drain
- D15 pad 2: /Solenoid_Iso/PhotoRelay7_Drain -> Net-(D15-A)
- D16 pad 1: /Solenoid_Iso/PhotoRelay4_Drain -> /Solenoid_Iso/PhotoRelay8_Drain
- D17 pad 1: +12V -> /MCU_stm32_g431k8t6/MCU_State_LED
- D17 pad 2: /Solenoid_Iso/PhotoRelay4_Drain -> Net-(D17-A)
- D18 pad 1: /Solenoid_Iso/PhotoRelay8_Drain -> /MCU_stm32_g431k8t6/FDCAN1_LED
- D19 pad 2: /Solenoid_Iso/PhotoRelay8_Drain -> GNDPWR
- D2 pad 1: /MCU_stm32_g431k8t6/FDCAN1_LED -> +12V
- D2 pad 2: Net-(D2-A) -> /Solenoid_Iso/Solenoid2_-
- D4 pad 1: /Solenoid_Iso/PhotoRelay1_Drain -> +12V
- D4 pad 2: Net-(D4-A) -> /Solenoid_Iso/PhotoRelay4_Drain
- D5 pad 2: /Solenoid_Iso/PhotoRelay1_Drain -> /Solenoid_Iso/PhotoRelay5_Drain
- D6 pad 1: /Solenoid_Iso/PhotoRelay5_Drain -> +12V
- D6 pad 2: Net-(D6-A) -> /Solenoid_Iso/PhotoRelay6_Drain
- D7 pad 2: /Solenoid_Iso/PhotoRelay5_Drain -> /Solenoid_Iso/PhotoRelay7_Drain
- D8 pad 1: /Solenoid_Iso/PhotoRelay2_Drain -> +12V
- D8 pad 2: Net-(D8-A) -> /Solenoid_Iso/PhotoRelay8_Drain
- D9 pad 1: +12V -> /Solenoid_Iso/PhotoRelay1_Drain
- D9 pad 2: /Solenoid_Iso/PhotoRelay2_Drain -> Net-(D9-A)
- IC2 pad 6: /Solenoid_Iso/PhotoRelay1_Drain -> /Solenoid_Iso/PhotoRelay2_Drain
- IC3 pad 6: /Solenoid_Iso/PhotoRelay2_Drain -> /Solenoid_Iso/PhotoRelay3_Drain
- IC4 pad 6: /Solenoid_Iso/PhotoRelay3_Drain -> /Solenoid_Iso/PhotoRelay4_Drain
- IC5 pad 6: /Solenoid_Iso/PhotoRelay4_Drain -> /Solenoid_Iso/PhotoRelay5_Drain
- IC6 pad 6: /Solenoid_Iso/PhotoRelay5_Drain -> /Solenoid_Iso/PhotoRelay6_Drain
- IC7 pad 6: /Solenoid_Iso/PhotoRelay6_Drain -> /Solenoid_Iso/PhotoRelay7_Drain
- IC8 pad 6: /Solenoid_Iso/PhotoRelay7_Drain -> /Solenoid_Iso/PhotoRelay8_Drain
- IC9 pad 1: Net-(IC9-A) -> GNDPWR
- IC9 pad 3: GND -> +24V
- IC9 pad 4: GNDPWR -> /FB
- IC9 pad 6: /Solenoid_Iso/PhotoRelay8_Drain -> Net-(IC9-BOOT)
- J10 pad 1: +12V -> /CANL
- J10 pad 2: GNDPWR -> /CANH
- J10 pad 3: /SPI_DAC/-VSENSE -> /CANL
- J10 pad 4: /SPI_DAC/VOUT -> +5V
- J10 pad 5: /SPI_DAC/+VSENSE -> +5V
- J10 pad 6: /SPI_ADC/VIN -> /CANH
- J13 pad 1: /CANL -> GNDPWR
- J13 pad 2: /CANH -> +24V
- J14 pad 1: unconnected-(J14-Pin_1-Pad1) -> +12V
- J14 pad 2: unconnected-(J14-Pin_2-Pad2) -> GNDPWR
- J14 pad 3: +3.3V -> /SPI_DAC/-VSENSE
- J14 pad 4: /MCU_stm32_g431k8t6/JTMS_SWDIO -> /SPI_DAC/VOUT
- J14 pad 5: GND -> /SPI_DAC/+VSENSE
- J14 pad 6: /MCU_stm32_g431k8t6/JTCK_SWCLK -> /SPI_ADC/VIN
- J2 pad 1: /Solenoid_Iso/PhotoRelay5_Drain -> /Solenoid_Iso/Solenoid2_-
- J3 pad 1: /Solenoid_Iso/PhotoRelay2_Drain -> /Solenoid_Iso/PhotoRelay3_Drain
- J4 pad 1: /Solenoid_Iso/PhotoRelay6_Drain -> /Solenoid_Iso/PhotoRelay4_Drain
- J5 pad 1: /Solenoid_Iso/PhotoRelay3_Drain -> /Solenoid_Iso/PhotoRelay5_Drain
- J6 pad 1: /Solenoid_Iso/PhotoRelay7_Drain -> /Solenoid_Iso/PhotoRelay6_Drain
- J7 pad 1: /Solenoid_Iso/PhotoRelay4_Drain -> /Solenoid_Iso/PhotoRelay7_Drain
- J8 pad 1: GNDPWR -> /Solenoid_Iso/PhotoRelay8_Drain
- J8 pad 2: +24V -> +12V
- J9 pad 1: /Solenoid_Iso/PhotoRelay8_Drain -> unconnected-(J9-Pin_1-Pad1)
- J9 pad 2: +12V -> unconnected-(J9-Pin_2-Pad2)
- R1 pad 1: +3.3V -> Net-(D9-A)
- R1 pad 2: Net-(D1-A) -> +12V
- R10 pad 2: Net-(IC3-A) -> Net-(IC2-A)
- R11 pad 2: Net-(IC4-A) -> Net-(IC3-A)
- R12 pad 2: Net-(IC5-A) -> Net-(IC4-A)
- R13 pad 2: Net-(IC6-A) -> Net-(IC5-A)
- R14 pad 2: Net-(IC7-A) -> Net-(IC6-A)
- R15 pad 2: Net-(IC8-A) -> Net-(IC7-A)
- R16 pad 2: Net-(IC9-A) -> Net-(IC8-A)
- R17 pad 1: Net-(D8-A) -> Net-(IC1-A)
- R17 pad 2: +12V -> GND
- R18 pad 1: Net-(D10-A) -> Net-(IC2-A)
- R18 pad 2: +12V -> GND
- R19 pad 1: Net-(D12-A) -> Net-(IC3-A)
- R19 pad 2: +12V -> GND
- R2 pad 1: +3.3V -> Net-(D10-A)
- R2 pad 2: Net-(D2-A) -> +12V
- R20 pad 1: Net-(D14-A) -> Net-(IC4-A)
- R20 pad 2: +12V -> GND
- R21 pad 1: Net-(D16-A) -> Net-(IC5-A)
- R21 pad 2: +12V -> GND
- R22 pad 1: Net-(D18-A) -> Net-(IC6-A)
- R22 pad 2: +12V -> GND
- R23 pad 1: Net-(IC9-A) -> Net-(IC7-A)
- R25 pad 1: Net-(IC7-A) -> /MCU_stm32_g431k8t6/BOOT0
- R26 pad 1: Net-(IC6-A) -> +3.3V
- R26 pad 2: GND -> Net-(D17-A)
- R27 pad 1: Net-(IC5-A) -> +3.3V
- R27 pad 2: GND -> Net-(D18-A)
- R28 pad 1: Net-(IC4-A) -> /MCU_stm32_g431k8t6/EP_Regu_DAC_CS
- R28 pad 2: GND -> /SPI_Iso/CS1_IN
- R29 pad 1: Net-(IC3-A) -> /MCU_stm32_g431k8t6/EP_Regu_ADC_CS
- R29 pad 2: GND -> /SPI_Iso/CS2_IN
- R30 pad 1: Net-(IC2-A) -> /MCU_stm32_g431k8t6/SPI1_SCK
- R30 pad 2: GND -> /SPI_Iso/CLK_IN
- R31 pad 1: /MCU_stm32_g431k8t6/BOOT0 -> /MCU_stm32_g431k8t6/SPI1_MOSI
- R31 pad 2: GND -> /SPI_Iso/MOSI_IN
- R32 pad 1: /SPI_DAC/+VSENSE -> /SPI_Iso/MISO_IN
- R32 pad 2: Net-(R32-Pad2) -> /SPI_ADC/MISO
- R33 pad 1: /SPI_DAC/-VSENSE -> Net-(U7-FB)
- R33 pad 2: Net-(R33-Pad2) -> +5VP
- R34 pad 1: Net-(R33-Pad2) -> Net-(U7-FB)
- R34 pad 2: Net-(U3-+) -> GNDPWR
- R35 pad 1: Net-(R32-Pad2) -> +12V
- R35 pad 2: Net-(U3--) -> /FB
- R36 pad 1: Net-(R32-Pad2) -> /FB
- R36 pad 2: /SPI_DAC/VOUT -> GNDPWR
- R37 pad 1: Net-(U3-+) -> +3.3V
- R37 pad 2: Net-(U2-VOUT) -> /SPI_Iso/CS1_IN
- R38 pad 1: Net-(R33-Pad2) -> +3.3V
- R38 pad 2: GNDPWR -> /SPI_Iso/CS2_IN
- R39 pad 1: GNDPWR -> /SPI_DAC/+VSENSE
- R39 pad 2: Net-(U3--) -> Net-(R39-Pad2)
- R40 pad 1: +3.3V -> /SPI_DAC/-VSENSE
- R40 pad 2: Net-(U4-VIA) -> Net-(R40-Pad2)
- R41 pad 1: +3.3V -> Net-(R40-Pad2)
- R41 pad 2: Net-(U4-VIB) -> /SPI_DAC/OP_VIN+
- R42 pad 1: /MCU_stm32_g431k8t6/EP_Regu_LATCH -> Net-(R39-Pad2)
- R42 pad 2: Net-(U4-VIA) -> /SPI_DAC/OP_VIN-
- R43 pad 1: /SPI_Iso/CS2_IN -> Net-(R39-Pad2)
- R43 pad 2: Net-(U4-VIB) -> /SPI_DAC/VOUT
- R44 pad 1: Net-(U4-VIE) -> /SPI_DAC/OP_VIN+
- R44 pad 2: /SPI_ADC/MISO -> Net-(U3-VOUT)
- R45 pad 1: /SPI_ADC/VIN -> Net-(R40-Pad2)
- R45 pad 2: Net-(U5-+) -> GNDPWR
- R46 pad 1: Net-(U5--) -> GNDPWR
- R46 pad 2: Net-(U6-AIN0) -> /SPI_DAC/OP_VIN-
- R47 pad 1: Net-(U5-+) -> /SPI_ADC/VIN
- R47 pad 2: GNDPWR -> Net-(U5-+)
- R5 pad 1: /MCU_stm32_g431k8t6/SPI1_SCK -> Net-(D13-A)
- R5 pad 2: /SPI_Iso/CLK_IN -> +12V
- R6 pad 1: /MCU_stm32_g431k8t6/SPI1_MOSI -> Net-(D14-A)
- R6 pad 2: /SPI_Iso/MOSI_IN -> +12V
- R7 pad 1: Net-(D4-A) -> Net-(D15-A)
- R8 pad 1: Net-(D6-A) -> Net-(D16-A)
- R9 pad 2: Net-(IC2-A) -> Net-(IC1-A)
- SW1 pad 1: /MCU_stm32_g431k8t6/ID_SW_BIT1 -> /MCU_stm32_g431k8t6/NRST
- SW1 pad 2: /MCU_stm32_g431k8t6/ID_SW_BIT2 -> GND
- SW2 pad 1: /MCU_stm32_g431k8t6/NRST -> /MCU_stm32_g431k8t6/ID_SW_BIT1
- SW2 pad 2: GND -> /MCU_stm32_g431k8t6/ID_SW_BIT2
- U1 pad 13: /MCU_stm32_g431k8t6/EP_Regu_LATCH -> /MCU_stm32_g431k8t6/EP_Regu_DAC_CS
- U1 pad 9: unconnected-(U1-PA4-Pad9) -> /MCU_stm32_g431k8t6/EP_Regu_ADC_CS
- U2 pad 1: +5VP -> +3.3V
- U2 pad 10: Net-(U2-VREFIO) -> unconnected-(U2-NIC-Pad10)
- U2 pad 2: Net-(U2-VOUT) -> /SPI_Iso/CS1_IN
- U2 pad 3: unconnected-(U2-NC-Pad3) -> /SPI_Iso/CS2_IN
- U2 pad 4: GND -> /SPI_Iso/CLK_IN
- U2 pad 5: GND -> /SPI_Iso/MOSI_IN
- U2 pad 6: /SPI_ADC/MOSI -> /SPI_Iso/MISO_OUT
- U2 pad 7: /SPI_DAC/CS_N -> unconnected-(U2-NIC-Pad7)
- U2 pad 8: /SPI_DAC/SDIN -> GND
- U2 pad 9: unconnected-(U2-NC-Pad9) -> GNDPWR
- U3 pad 1: /SPI_DAC/VOUT -> +5VP
- U3 pad 2: GNDPWR -> Net-(U3-VOUT)
- U3 pad 3: Net-(U3-+) -> unconnected-(U3-NC-Pad3)
- U3 pad 4: Net-(U3--) -> GNDPWR
- U3 pad 5: +12V -> GNDPWR
- U4 pad 1: +3.3V -> /SPI_DAC/VOUT
- U4 pad 2: Net-(U4-VIA) -> GNDPWR
- U4 pad 3: Net-(U4-VIB) -> /SPI_DAC/OP_VIN+
- U4 pad 4: /SPI_Iso/CLK_IN -> /SPI_DAC/OP_VIN-
- U4 pad 5: /SPI_Iso/MOSI_IN -> +12V
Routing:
- net +12V: track 19.8 -> 0.00 mm, vias 2 -> 0
- net /FB: track 9.20 -> 0.00 mm, vias 2 -> 0
- net +24V: track 8.88 -> 0.00 mm
- net Net-(IC1-SW): track 8.83 -> 0.00 mm, vias 2 -> 0
- net GNDPWR: track 2.25 -> 0.00 mm, vias 3 -> 0
- net Net-(IC1-BOOT): track 1.89 -> 0.00 mm
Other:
- board text added: "<-SENSE:LOCAL->"

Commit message: working
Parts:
- C20, C21, D1, D2, D3, D4, D5, D6, D7, D8, R1, R18, R19, R2, R20, R21, R22, R23, R24, R3, R37, R38, R4, R5, R6, R7, R8: moved to B.Cu
- C3, R28, R29, R9: moved to F.Cu
- moved J12 80.3 mm to (192.2, 108.8)
- moved R47 63.3 mm to (142.7, 110.3), turned to 0 degrees
- moved R49 63.0 mm to (142.7, 108.6), turned to 180 degrees
- moved C24 62.9 mm to (142.7, 106.8), turned to 180 degrees
- moved U5 62.2 mm to (142.2, 103.8), turned to 90 degrees
- moved D19 60.2 mm to (119.8, 79.8), turned to -90 degrees
- moved C23 60.0 mm to (139.2, 92.8), turned to 180 degrees
- moved R48 58.7 mm to (139.7, 103.3), turned to 90 degrees
- moved U6 58.6 mm to (139.2, 97.5), turned to 90 degrees
- moved C25 56.5 mm to (138.2, 103.3), turned to -90 degrees
- moved C12 56.0 mm to (117.8, 79.8), turned to -90 degrees
- moved C11 54.7 mm to (116.2, 79.8), turned to -90 degrees
- moved C7 54.3 mm to (183.8, 88.8), turned to -90 degrees
- moved C9 53.1 mm to (118.8, 68.2)
- moved C10 52.6 mm to (118.8, 69.8)
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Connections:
- D10 pad 1: /Solenoid_Iso/Solenoid2_- -> /Solenoid_Iso/PhotoRelay2_Drain
- D2 pad 2: /Solenoid_Iso/Solenoid2_- -> /Solenoid_Iso/PhotoRelay2_Drain
- J2 pad 1: /Solenoid_Iso/Solenoid2_- -> /Solenoid_Iso/PhotoRelay2_Drain
- U2 pad 12: /SPI_Iso/MOSI_OUT -> /SPI_ADC/MOSI
- U2 pad 13: /SPI_Iso/CLK_OUT -> /SPI_ADC/SCLK
- U2 pad 6: /SPI_Iso/MISO_OUT -> /MCU_stm32_g431k8t6/SPI1_MISO
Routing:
- net +12V: track 0.00 -> 173.6 mm, vias 0 -> 1
- net +3.3V: track 0.00 -> 78.2 mm, vias 0 -> 2
- net +5V: track 0.00 -> 54.6 mm, vias 0 -> 1
- net /CANL: track 0.00 -> 51.2 mm, vias 0 -> 3
- net /CANH: track 0.00 -> 44.0 mm
- net /MCU_stm32_g431k8t6/Solenoid8_GPIO: track 0.00 -> 37.8 mm
- net /MCU_stm32_g431k8t6/Solenoid7_GPIO: track 0.00 -> 28.7 mm
- net /MCU_stm32_g431k8t6/Solenoid1_GPIO: track 0.00 -> 27.1 mm, vias 0 -> 2
- net +24V: track 0.00 -> 20.8 mm
- net /MCU_stm32_g431k8t6/Solenoid6_GPIO: track 0.00 -> 19.7 mm
- net /MCU_stm32_g431k8t6/Solenoid2_GPIO: track 0.00 -> 19.1 mm, vias 0 -> 2
- net /MCU_stm32_g431k8t6/SPI1_MOSI: track 0.00 -> 17.3 mm, vias 0 -> 2
- net /SPI_DAC/+VSENSE: track 0.00 -> 16.6 mm, vias 0 -> 1
- net /MCU_stm32_g431k8t6/SPI1_MISO: track 0.00 -> 16.6 mm, vias 0 -> 3
- net /MCU_stm32_g431k8t6/JTMS_SWDIO: track 0.00 -> 16.4 mm, vias 0 -> 2
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- added copper zone on B.Cu, net GND
- added copper zone on F.Cu, net GND
- added copper zone on B.Cu, net GNDPWR
- added copper zone on F.Cu, net GNDPWR
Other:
- board outline added: 95.5 x 61.8 mm
- board text added: "<-SENSE|LOCAL-> value: 0Ω"
- board text added: "DAC FB Setting"
- board text removed: "<-SENSE:LOCAL->"
